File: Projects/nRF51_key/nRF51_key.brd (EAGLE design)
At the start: 160 x 100 mm, 4 parts, among them IC1 FT230XQ, X1 USBPCB

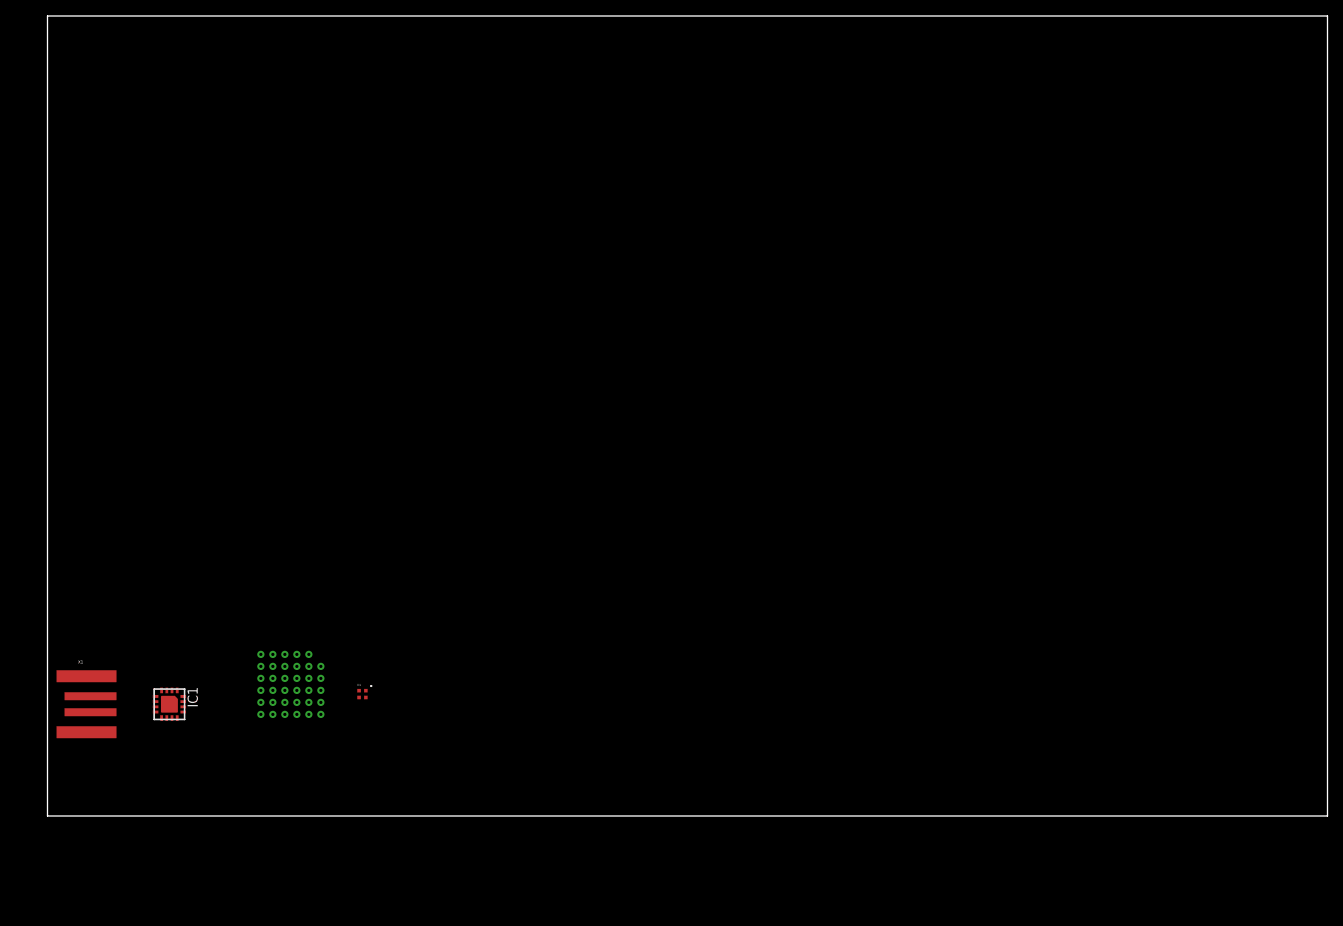
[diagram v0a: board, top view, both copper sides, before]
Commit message: More on the nRF51 USB key
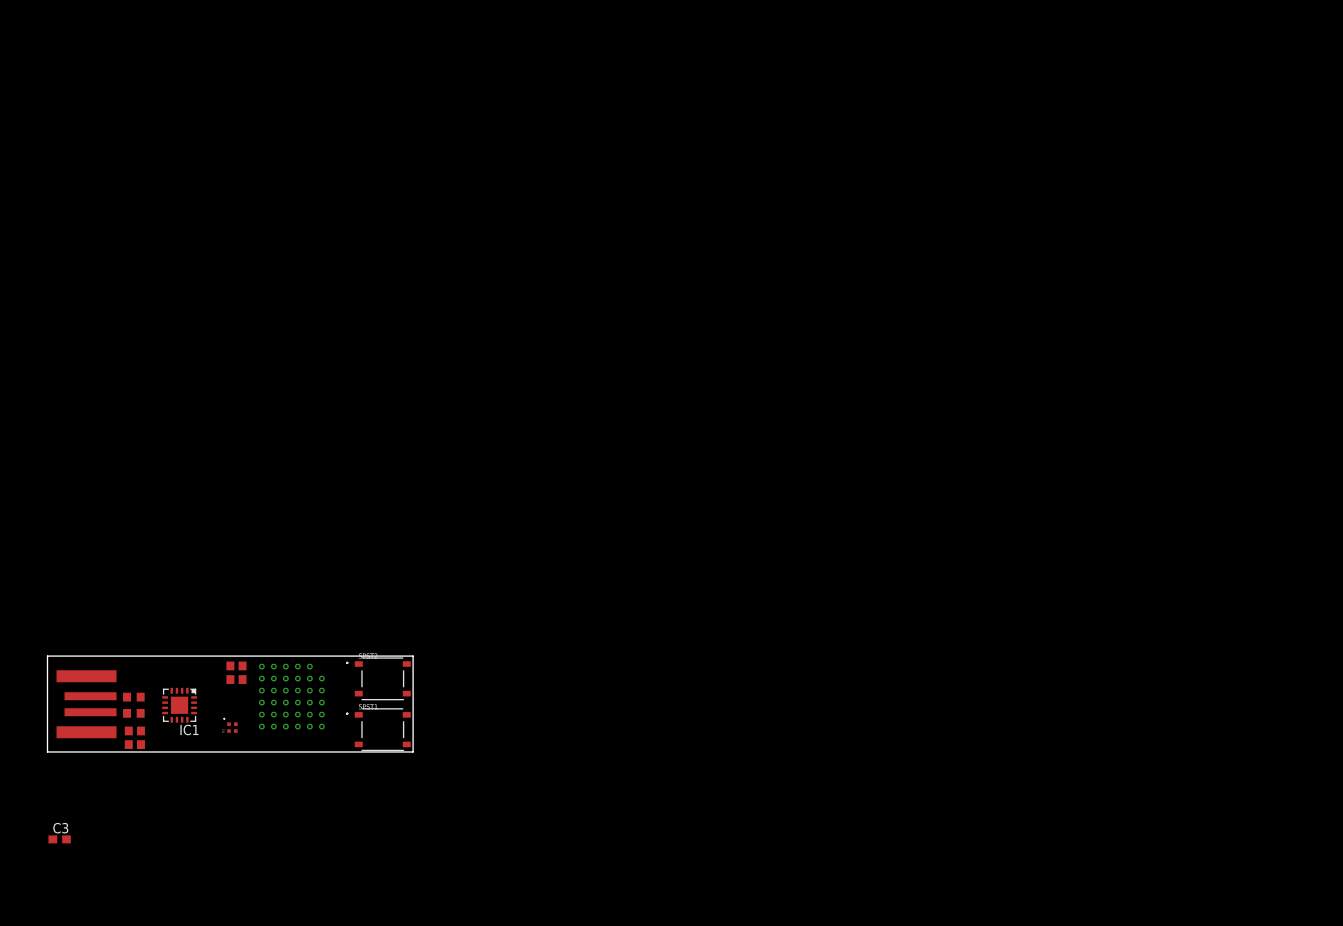
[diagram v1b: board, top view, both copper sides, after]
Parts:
- added C1: 10uF, Passives:C0603
- added C2, C5: 100nF, Passives:C0603
- added C3: (no value), Passives:C0603
- added C4: 4.7uF, Passives:C0603
- added R1, R2: (no value), Passives:R0603
- added SPST1, SPST2: PTS526SK08, SPST:PTS526SKG15SMTR2LFS
- IC1: device ftdichip:QFN16 -> FTDI:QFN16
- moved D1 16.8 mm to (23.1, 11.0), turned to 90 degrees
- moved U$1 1.53 mm to (26.8, 11.2)
- moved IC1 1.28 mm to (16.5, 13.8)
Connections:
- removed net !RESET: IC1.9
- removed net 3V3OUT: IC1.8, U$1.B5, U$1.B6, U$1.C5, U$1.C6
- removed net CBUS0: IC1.12
- removed net CBUS1: IC1.11
- removed net CBUS2: IC1.5
- removed net CBUS3: IC1.14
- removed net VCC: IC1.10
- removed net VCCIO: IC1.1
- new net BTN1: SPST1.1, SPST1.2
- new net BTN2: SPST2.1, SPST2.2
- new net IC1_USBDM: IC1.7, R1.2
- new net IC1_USBDP: IC1.6, R2.2
- new net VDD: C4.1, C5.1, D1.1, IC1.1, IC1.8, IC1.9, U$1.B5, U$1.B6, U$1.C5, U$1.C6
- net GND: now also C1.2, C2.2, C3.2, C4.2, C5.2, IC1.EXP, SPST1.3, SPST1.4, SPST2.3, SPST2.4
- net USBDM: now also R1.1; no longer IC1.7
- net USBDP: now also R2.1; no longer IC1.6
- net VBUS: now also C1.1, C2.1, IC1.10
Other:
- board size 160 x 100 mm -> 45.7 x 12 mm

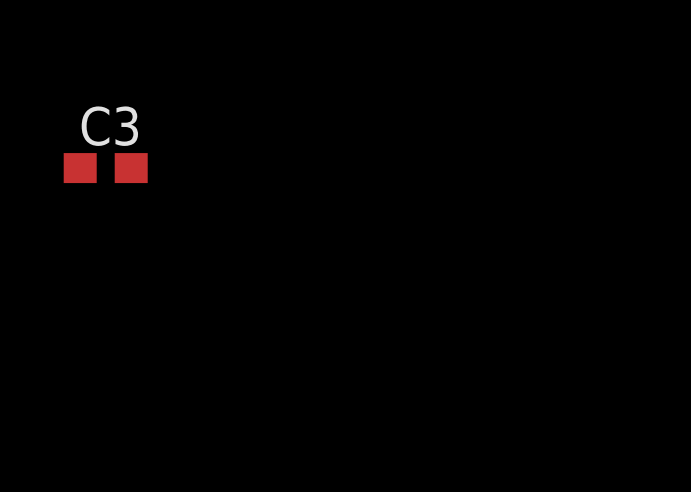
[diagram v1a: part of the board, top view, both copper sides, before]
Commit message: Added PCB SD card symbol
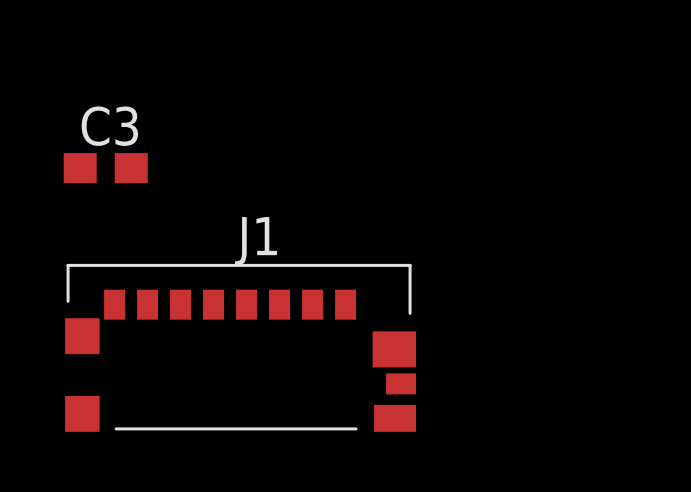
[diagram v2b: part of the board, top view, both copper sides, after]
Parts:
- added J1: 47571-0001, SD_Card:47571-0001
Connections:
- new net CLK: J1.5
- new net CS: J1.2
- new net MISO: J1.7
- new net MOSI: J1.3
- new net SWDCLK: J1.8, U$1.SWDCLK
- new net SWDIO: J1.1, U$1.SWDIO
- net GND: now also J1.10, J1.11, J1.12, J1.13, J1.6, J1.9
- net VDD: now also J1.4
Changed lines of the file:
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@@
 <layer number="54" name="bGND_GNDA" color="1" fill="9" visible="no" active="no"/>
 <layer number="56" name="wert" color="7" fill="1" visible="no" active="no"/>
+<layer number="57" name="tCAD" color="7" fill="1" visible="no" active="no"/>
+<layer number="59" name="tCarbon" color="7" fill="1" visible="no" active="no"/>
+<layer number="60" name="bCarbon" color="7" fill="1" visible="no" active="no"/>
 <layer number="88" name="SimResults" color="9" fill="1" visible="no" active="no"/>
 <layer number="89" name="SimProbes" color="9" fill="1" visible="no" active="no"/>
@@
 <layer number="125" name="_tNames" color="7" fill="1" visible="no" active="yes"/>
 <layer number="126" name="BIFRNTMAT" color="7" fill="1" visible="yes" active="yes"/>
+<layer number="127" name="_tValues" color="7" fill="1" visible="no" active="no"/>
+<layer number="128" name="_bValues" color="7" fill="1" visible="no" active="no"/>
+<layer number="129" name="Mask" color="7" fill="1" visible="no" active="no"/>
 <layer number="130" name="SMDSTROOK" color="7" fill="1" visible="yes" active="yes"/>
 <layer number="131" name="tAdjust" color="7" fill="1" visible="yes" active="yes"/>
 <layer number="132" name="bAdjust" color="7" fill="1" visible="yes" active="yes"/>
 <layer number="144" name="Drill_legend" color="7" fill="1" visible="no" active="yes"/>
+<layer number="150" name="Notes" color="7" fill="1" visible="no" active="no"/>
 <layer number="151" name="HeatSink" color="7" fill="1" visible="no" active="yes"/>
+<layer number="152" name="_bDocu" color="7" fill="1" visible="no" active="no"/>
+<layer number="153" name="FabDoc1" color="7" fill="1" visible="no" active="no"/>
+<layer number="154" name="FabDoc2" color="7" fill="1" visible="no" active="no"/>
+<layer number="155" name="FabDoc3" color="7" fill="1" visible="no" active="no"/>
 <layer number="199" name="Contour" color="7" fill="1" visible="yes" active="yes"/>
 <layer number="200" name="200bmp" color="1" fill="10" visible="no" active="yes"/>
@@
 <layer number="223" name="223bmp" color="24" fill="1" visible="no" active="no"/>
 <layer number="224" name="224bmp" color="25" fill="1" visible="no" active="no"/>
+<layer number="225" name="225bmp" color="7" fill="1" visible="no" active="no"/>
+<layer number="226" name="226bmp" color="7" fill="1" visible="no" active="no"/>
+<layer number="227" name="227bmp" color="7" fill="1" visible="no" active="no"/>
+<layer number="228" name="228bmp" color="7" fill="1" visible="no" active="no"/>
+<layer number="229" name="229bmp" color="7" fill="1" visible="no" active="no"/>
+<layer number="230" name="230bmp" color="7" fill="1" visible="no" active="no"/>
+<layer number="231" name="231bmp" color="7" fill="1" visible="no" active="no"/>
+<layer number="232" name="Eagle3D_PG2" color="7" fill="1" visible="no" active="no"/>
+<layer number="233" name="Eagle3D_PG3" color="7" fill="1" visible="no" active="no"/>
+<layer number="248" name="Housing" color="7" fill="1" visible="no" active="no"/>
+<layer number="249" name="Edge" color="7" fill="1" visible="no" active="no"/>
 <layer number="250" name="Descript" color="3" fill="1" visible="no" active="no"/>
 <layer number="251" name="SMDround" color="12" fill="11" visible="no" active="no"/>
@@
 <attribute name="VALUE" x="9.906" y="12.827" size="1.27" layer="27"/>
 </element>
+<element name="J1" library="SD_Card" package="47571-0001" value="47571-0001" x="5.969" y="-8.89" smashed="yes">
+<attribute name="NAME" x="6.645" y="-5.189" size="1.27" layer="25" align="center"/>
+<attribute name="VALUE" x="5.883" y="-12.555" size="1.27" layer="27" align="center"/>
+</element>
 </elements>
 <signals>
@@
 <contactref element="C2" pad="2"/>
 <contactref element="C1" pad="2"/>
+<contactref element="J1" pad="6"/>
+<contactref element="J1" pad="13"/>
+<contactref element="J1" pad="11"/>
+<contactref element="J1" pad="12"/>
+<contactref element="J1" pad="9"/>
+<contactref element="J1" pad="10"/>
 <wire x1="38.91" y1="15.295" x2="44.91" y2="15.295" width="0" layer="19" extent="1-1"/>
 <wire x1="44.91" y1="8.945" x2="44.91" y2="15.295" width="0" layer="19" extent="1-1"/>
@@
 <wire x1="24.384" y1="18.757" x2="26.797" y2="18.676" width="0" layer="19" extent="1-1"/>
 <wire x1="22.86" y1="18.757" x2="24.384" y2="18.757" width="0" layer="19" extent="1-1"/>
-<wire x1="18.3225" y1="12.868" x2="22.86" y2="18.757" width="0" layer="19" extent="1-1"/>
-<wire x1="16.51" y1="13.843" x2="18.3225" y2="12.868" width="0" layer="19" extent="1-1"/>
-<wire x1="16.185" y1="15.6555" x2="16.51" y2="13.843" width="0" layer="19" extent="1-1"/>
+<wire x1="16.185" y1="15.6555" x2="22.86" y2="18.757" width="0" layer="19" extent="1-1"/>
+<wire x1="16.51" y1="13.843" x2="16.185" y2="15.6555" width="0" layer="19" extent="1-1"/>
+<wire x1="18.3225" y1="12.868" x2="16.51" y2="13.843" width="0" layer="19" extent="1-1"/>
 <wire x1="11.684" y1="8.929" x2="16.51" y2="13.843" width="0" layer="19" extent="1-1"/>
 <wire x1="10.16" y1="8.929" x2="11.684" y2="8.929" width="0" layer="19" extent="1-1"/>
 <wire x1="4.88" y1="17.47" x2="10.16" y2="8.929" width="0" layer="19" extent="1-1"/>
 <wire x1="2.374" y1="-2.921" x2="10.16" y2="8.929" width="0" layer="19" extent="1-1"/>
+<wire x1="0.744" y1="-8.525" x2="2.374" y2="-2.921" width="0" layer="19" extent="1-1"/>
+<wire x1="0.744" y1="-11.115" x2="0.744" y2="-8.525" width="0" layer="19" extent="1-1"/>
+<wire x1="7.319" y1="-7.475" x2="0.744" y2="-8.525" width="0" layer="19" extent="1-1"/>
+<wire x1="11.144" y1="-8.965" x2="7.319" y2="-7.475" width="0" layer="19" extent="1-1"/>
+<wire x1="11.369" y1="-10.115" x2="11.144" y2="-8.965" width="0" layer="19" extent="1-1"/>
+<wire x1="11.169" y1="-11.265" x2="11.369" y2="-10.115" width="0" layer="19" extent="1-1"/>
 </signal>
 <signal name="USBDP">
@@
 <contactref element="IC1" pad="9"/>
 <contactref element="IC1" pad="1"/>
+<contactref element="J1" pad="4"/>
+<wire x1="28.297" y1="15.676" x2="28.297" y2="17.176" width="0" layer="19" extent="1-1"/>
 <wire x1="26.797" y1="17.176" x2="28.297" y2="17.176" width="0" layer="19" extent="1-1"/>
-<wire x1="28.297" y1="15.676" x2="28.297" y2="17.176" width="0" layer="19" extent="1-1"/>
-<wire x1="26.797" y1="15.676" x2="26.797" y2="17.176" width="0" layer="19" extent="1-1"/>
+<wire x1="26.797" y1="15.676" x2="28.297" y2="15.676" width="0" layer="19" extent="1-1"/>
 <wire x1="24.384" y1="17.057" x2="26.797" y2="17.176" width="0" layer="19" extent="1-1"/>
 <wire x1="22.86" y1="17.057" x2="24.384" y2="17.057" width="0" layer="19" extent="1-1"/>
-<wire x1="22.689" y1="11.474" x2="22.86" y2="17.057" width="0" layer="19" extent="1-1"/>
 <wire x1="17.485" y1="15.6555" x2="22.86" y2="17.057" width="0" layer="19" extent="1-1"/>
 <wire x1="14.6975" y1="12.868" x2="17.485" y2="15.6555" width="0" layer="19" extent="1-1"/>
 <wire x1="15.535" y1="12.0305" x2="14.6975" y2="12.868" width="0" layer="19" extent="1-1"/>
+<wire x1="22.689" y1="11.474" x2="22.86" y2="17.057" width="0" layer="19" extent="1-1"/>
+<wire x1="5.119" y1="-7.475" x2="15.535" y2="12.0305" width="0" layer="19" extent="1-1"/>
 </signal>
 <signal name="BTN1">
@@
 <wire x1="11.645" y1="14.859" x2="14.6975" y2="14.168" width="0" layer="19" extent="1-1"/>
 </signal>
+<signal name="MISO">
+<contactref element="J1" pad="7"/>
+</signal>
+<signal name="CLK">
+<contactref element="J1" pad="5"/>
+</signal>
+<signal name="MOSI">
+<contactref element="J1" pad="3"/>
+</signal>
+<signal name="CS">
+<contactref element="J1" pad="2"/>
+</signal>
+<signal name="SWDIO">
+<contactref element="U$1" pad="SWDIO"/>
+<contactref element="J1" pad="1"/>
+<wire x1="1.819" y1="-7.475" x2="34.297" y2="17.176" width="0" layer="19" extent="1-1"/>
+</signal>
+<signal name="SWDCLK">
+<contactref element="U$1" pad="SWDCLK"/>
+<contactref element="J1" pad="8"/>
+<wire x1="9.519" y1="-7.475" x2="34.297" y2="15.676" width="0" layer="19" extent="1-1"/>
+</signal>
 </signals>
